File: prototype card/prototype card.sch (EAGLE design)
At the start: 21 parts, among them J1 09231486921, J2 TBP02R1-381-14BE

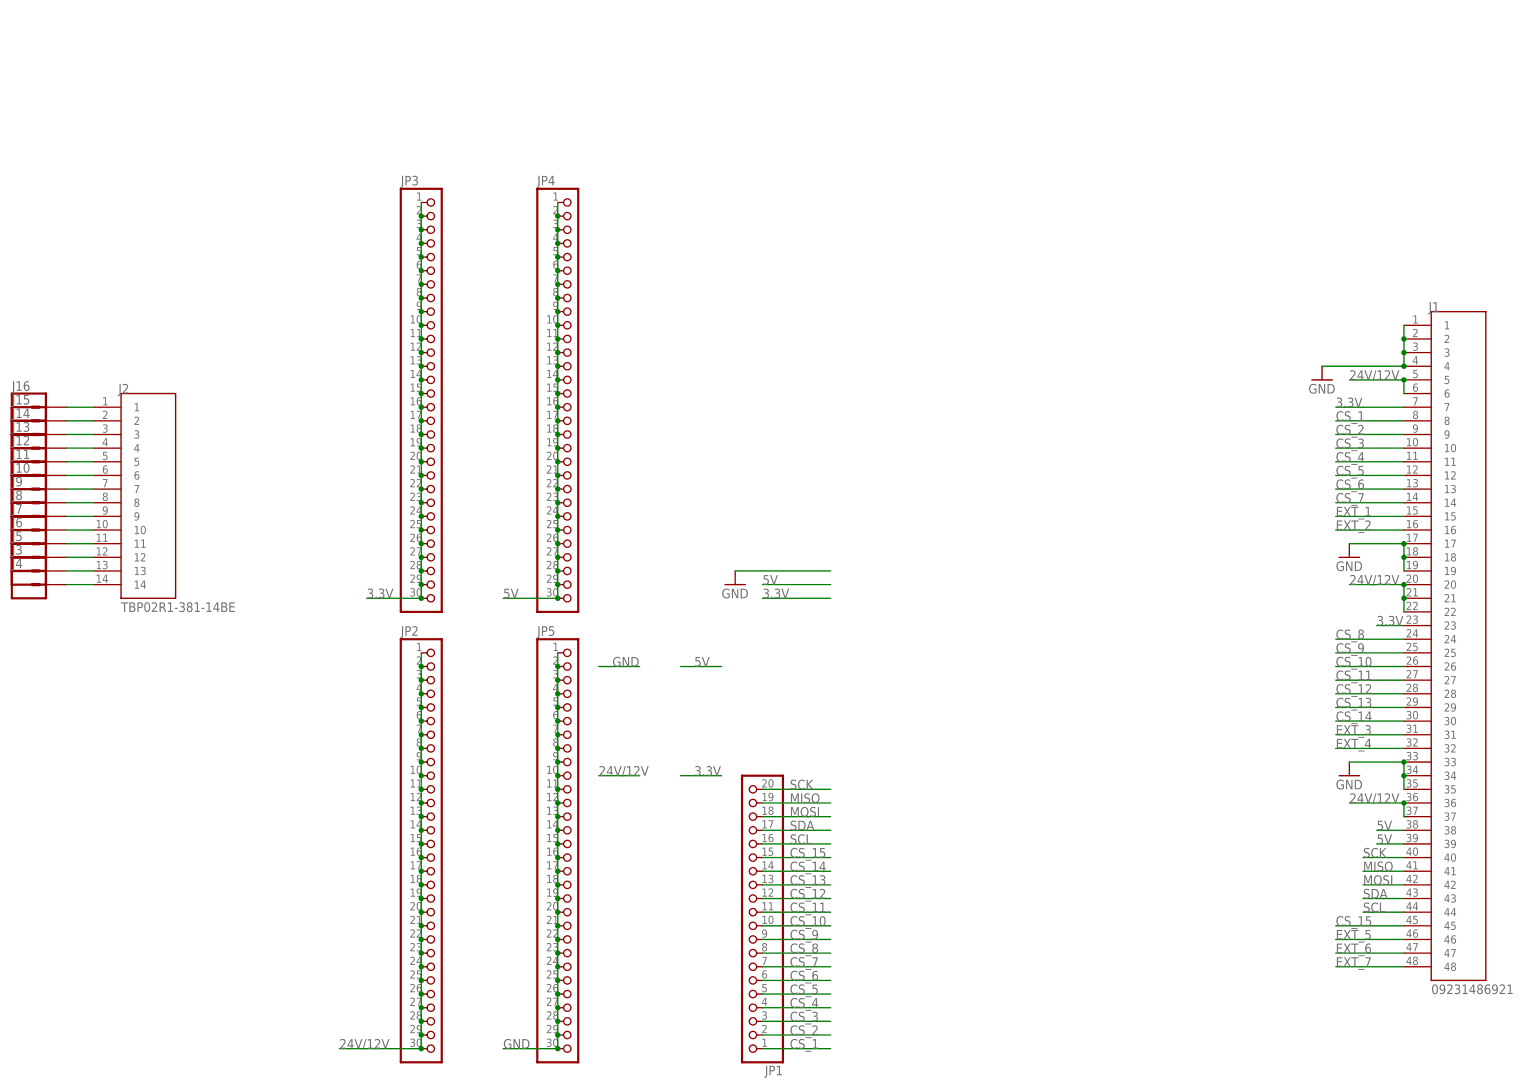
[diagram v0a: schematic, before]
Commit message: changed pinouts for the boards, next I have to make accomodations for new pinouts and the USB selector system
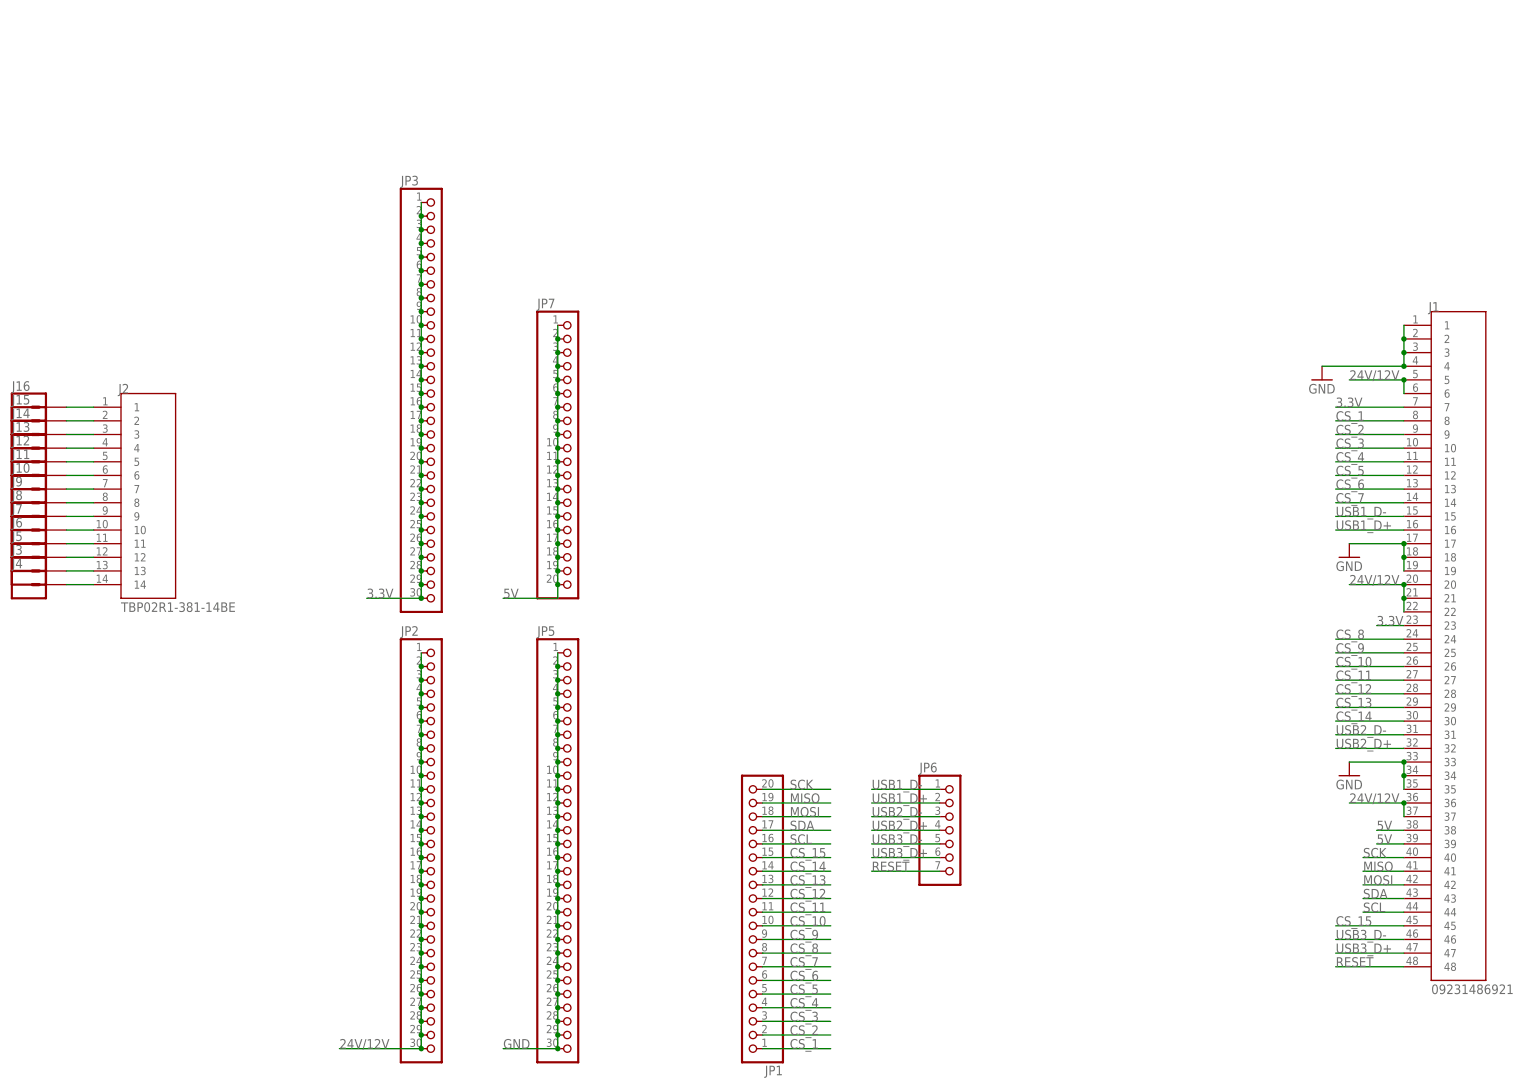
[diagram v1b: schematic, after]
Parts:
- removed JP4: (no value), pinhead:PINHD-1X30
- added JP6: (no value), pinhead:PINHD-1X7
- added JP7: (no value), pinhead:PINHD-1X20
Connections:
- removed net EXT_1: J1.15
- removed net EXT_2: J1.16
- removed net EXT_3: J1.31
- removed net EXT_4: J1.32
- removed net EXT_5: J1.46
- removed net EXT_6: J1.47
- removed net EXT_7: J1.48
- new net RESET: J1.48, JP6.7
- new net USB1_D+: J1.16, JP6.2
- new net USB1_D-: J1.15, JP6.1
- new net USB2_D+: J1.32, JP6.4
- new net USB2_D-: J1.31, JP6.3
- new net USB3_D+: J1.47, JP6.6
- new net USB3_D-: J1.46, JP6.5
- net 5V: now also JP7.1, JP7.10, JP7.11, JP7.12, JP7.13, JP7.14, JP7.15, JP7.16, JP7.17, JP7.18, JP7.19, JP7.2, JP7.20, JP7.3, JP7.4, JP7.5, JP7.6, JP7.7, JP7.8, JP7.9; no longer JP4.1, JP4.10, JP4.11, JP4.12, JP4.13, JP4.14, JP4.15, JP4.16, JP4.17, JP4.18, JP4.19, JP4.2, JP4.20, JP4.21, JP4.22, JP4.23, JP4.24, JP4.25, JP4.26, JP4.27, JP4.28, JP4.29, JP4.3, JP4.30, JP4.4, JP4.5, JP4.6, JP4.7, JP4.8, JP4.9

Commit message: made card holes bigger, started usb port work, but I'm not done that part yet
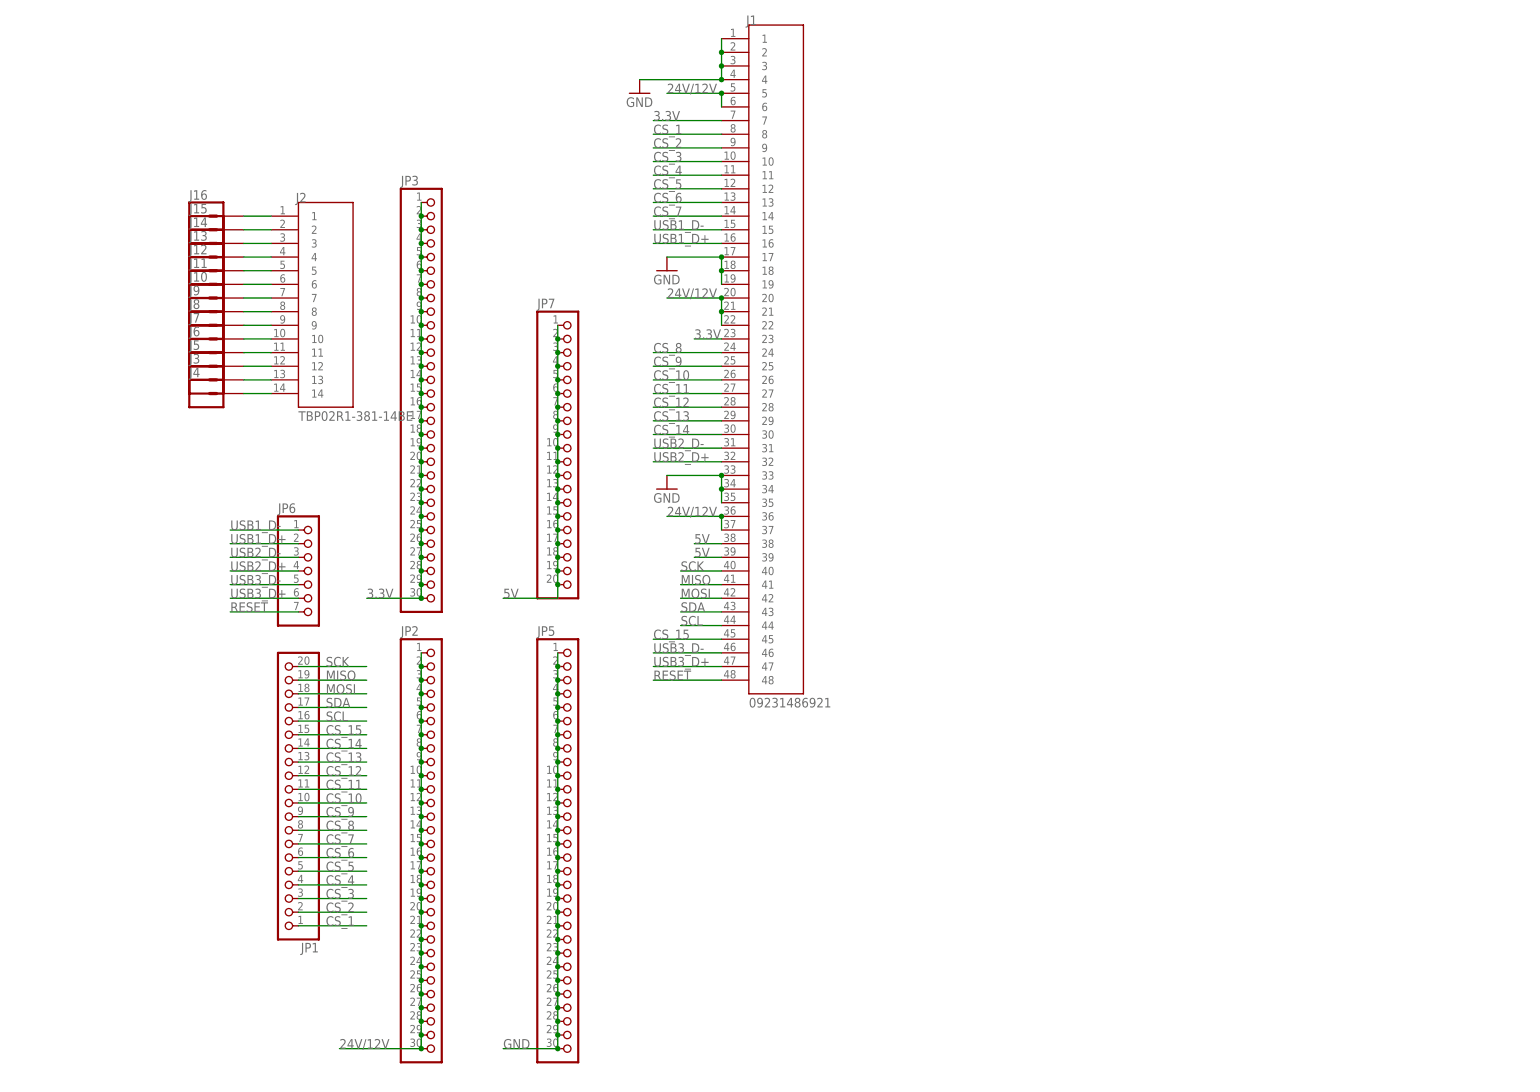
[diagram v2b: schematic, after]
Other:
- moved on the sheet: J1, J10, J11, J12, J13, J14, J15, J16, J2, J3, J4, J5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
